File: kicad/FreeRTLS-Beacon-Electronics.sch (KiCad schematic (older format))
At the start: 0 parts

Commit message: Add DWM USB and STM to sch
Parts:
- added D?: PMEG3020EH, Diode_SMD:D_SOD-123F, symbol Diode:PMEG3020EH
- added J?: USB_B_Micro, symbol Connector:USB_B_Micro
- added U?: DWM1001, RF_Module:DecaWave_DWM1001, symbol RF_Module:DWM1001
- added U?: STM32F072CBTx, Package_QFP:LQFP-48_7x7mm_P0.5mm, symbol MCU_ST_STM32F0:STM32F072CBTx
- added U?: NCP1117-3.3_SOT223, Package_TO_SOT_SMD:SOT-223-3_TabPin2, symbol Regulator_Linear:NCP1117-3.3_SOT223
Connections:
- new net: U?.1 (GND), U?.11 (GND), U?.24 (GND), U?.34 (GND)
- new net: D?.2 (A), J?.1 (VBUS)
- new net: D?.1 (K), U?.3 (VI)
- no-connect marks 0 -> 28
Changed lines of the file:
@@
 Sheet 1 1
 Title "FreeRTLS Beacon Electronics"
-Date "2020-08-27"
+Date "2020-09-01"
 Rev "WIP!"
 Comp "FreeRTLS"
@@
 Comment4 ""
 $EndDescr
+$Comp
+L RF_Module:DWM1001 U?
+U 1 1 5F4EAC7B
+P 6400 2750
+F 0 "U?" H 6400 4031 50  0000 C CNN
+F 1 "DWM1001" H 6400 3940 50  0000 C CNN
+F 2 "RF_Module:DecaWave_DWM1001" H 7100 1800 50  0001 C CNN
+F 3 "https://www.decawave.com/sites/default/files/dwm1001_datasheet.pdf" H 7300 1950 50  0001 C CNN
+	1    6400 2750
+	1    0    0    -1
+$EndComp
+$Comp
+L MCU_ST_STM32F0:STM32F072CBTx U?
+U 1 1 5F4EB7E0
+P 4800 5600
+F 0 "U?" H 4750 4011 50  0000 C CNN
+F 1 "STM32F072CBTx" H 4750 3920 50  0000 C CNN
+F 2 "Package_QFP:LQFP-48_7x7mm_P0.5mm" H 4200 4200 50  0001 R CNN
+F 3 "http://www.st.com/st-web-ui/static/active/en/resource/technical/document/datasheet/DM00090510.pdf" H 4800 5600 50  0001 C CNN
+	1    4800 5600
+	1    0    0    -1
+$EndComp
+$Comp
+L Connector:USB_B_Micro J?
+U 1 1 5F4ED800
+P 1650 2900
+F 0 "J?" H 1707 3367 50  0000 C CNN
+F 1 "USB_B_Micro" H 1707 3276 50  0000 C CNN
+F 2 "" H 1800 2850 50  0001 C CNN
+F 3 "~" H 1800 2850 50  0001 C CNN
+	1    1650 2900
+	1    0    0    -1
+$EndComp
+$Comp
+L Regulator_Linear:NCP1117-3.3_SOT223 U?
+U 1 1 5F4F1B06
+P 3200 2700
+F 0 "U?" H 3200 2942 50  0000 C CNN
+F 1 "NCP1117-3.3_SOT223" H 3200 2851 50  0000 C CNN
+F 2 "Package_TO_SOT_SMD:SOT-223-3_TabPin2" H 3200 2900 50  0001 C CNN
+F 3 "http://www.onsemi.com/pub_link/Collateral/NCP1117-D.PDF" H 3300 2450 50  0001 C CNN
+	1    3200 2700
+	1    0    0    -1
+$EndComp
+NoConn ~ 4100 5400
+NoConn ~ 4100 5500
+NoConn ~ 4100 5600
+NoConn ~ 4100 5700
+NoConn ~ 4100 5800
+NoConn ~ 4100 5900
+NoConn ~ 4100 6000
+NoConn ~ 4100 6100
+NoConn ~ 4100 6200
+NoConn ~ 4100 6300
+NoConn ~ 4100 6400
+NoConn ~ 4100 6500
+NoConn ~ 4100 6600
+NoConn ~ 4100 6700
+NoConn ~ 4100 6800
+NoConn ~ 4100 6900
+NoConn ~ 4100 5000
+NoConn ~ 4100 5100
+NoConn ~ 4100 5200
+NoConn ~ 4100 4700
+NoConn ~ 4100 4800
+NoConn ~ 5400 6200
+NoConn ~ 5400 5900
+NoConn ~ 5400 6000
+NoConn ~ 5400 6100
+NoConn ~ 5400 5700
+NoConn ~ 5400 6900
+NoConn ~ 1950 3100
+$Comp
+L Diode:PMEG3020EH D?
+U 1 1 5F4FD35F
+P 2200 2700
+F 0 "D?" H 2200 2484 50  0000 C CNN
+F 1 "PMEG3020EH" H 2200 2575 50  0000 C CNN
+F 2 "Diode_SMD:D_SOD-123F" H 2200 2525 50  0001 C CNN
+F 3 "https://assets.nexperia.com/documents/data-sheet/PMEG3020EH_EJ.pdf" H 2200 2700 50  0001 C CNN
+	1    2200 2700
+	-1   0    0    1
+$EndComp
+Wire Wire Line
+	1950 2700 2050 2700
+Wire Wire Line
+	2350 2700 2900 2700
 $EndSCHEMATC

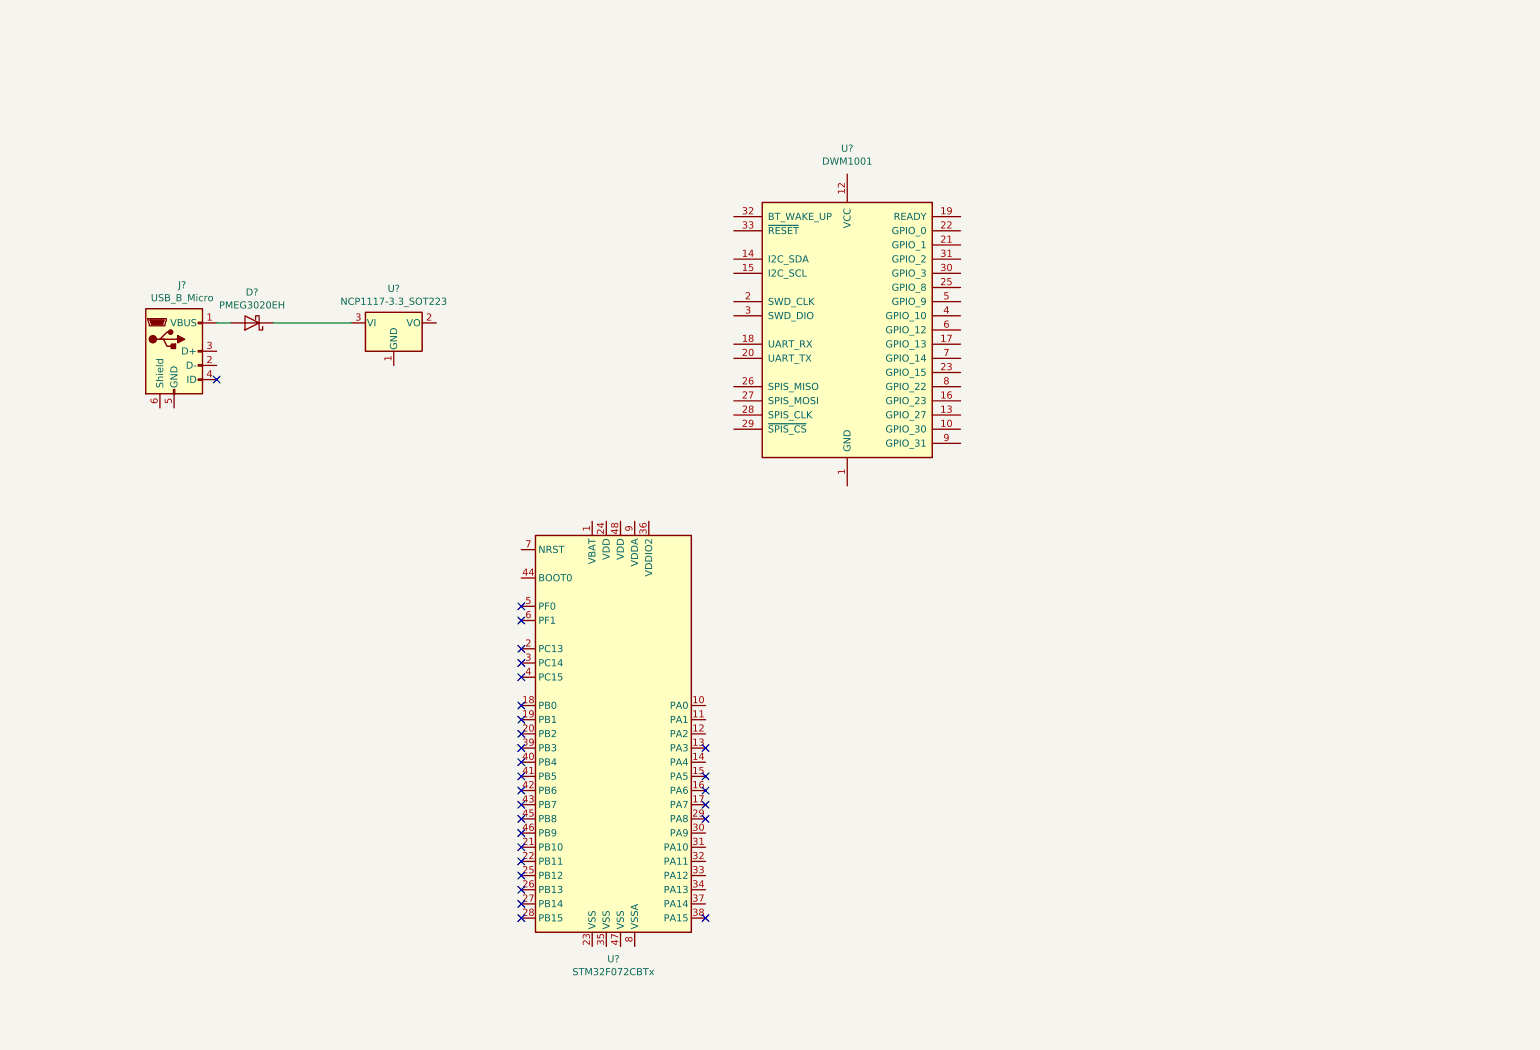
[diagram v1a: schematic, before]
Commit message: Add STM32 connections
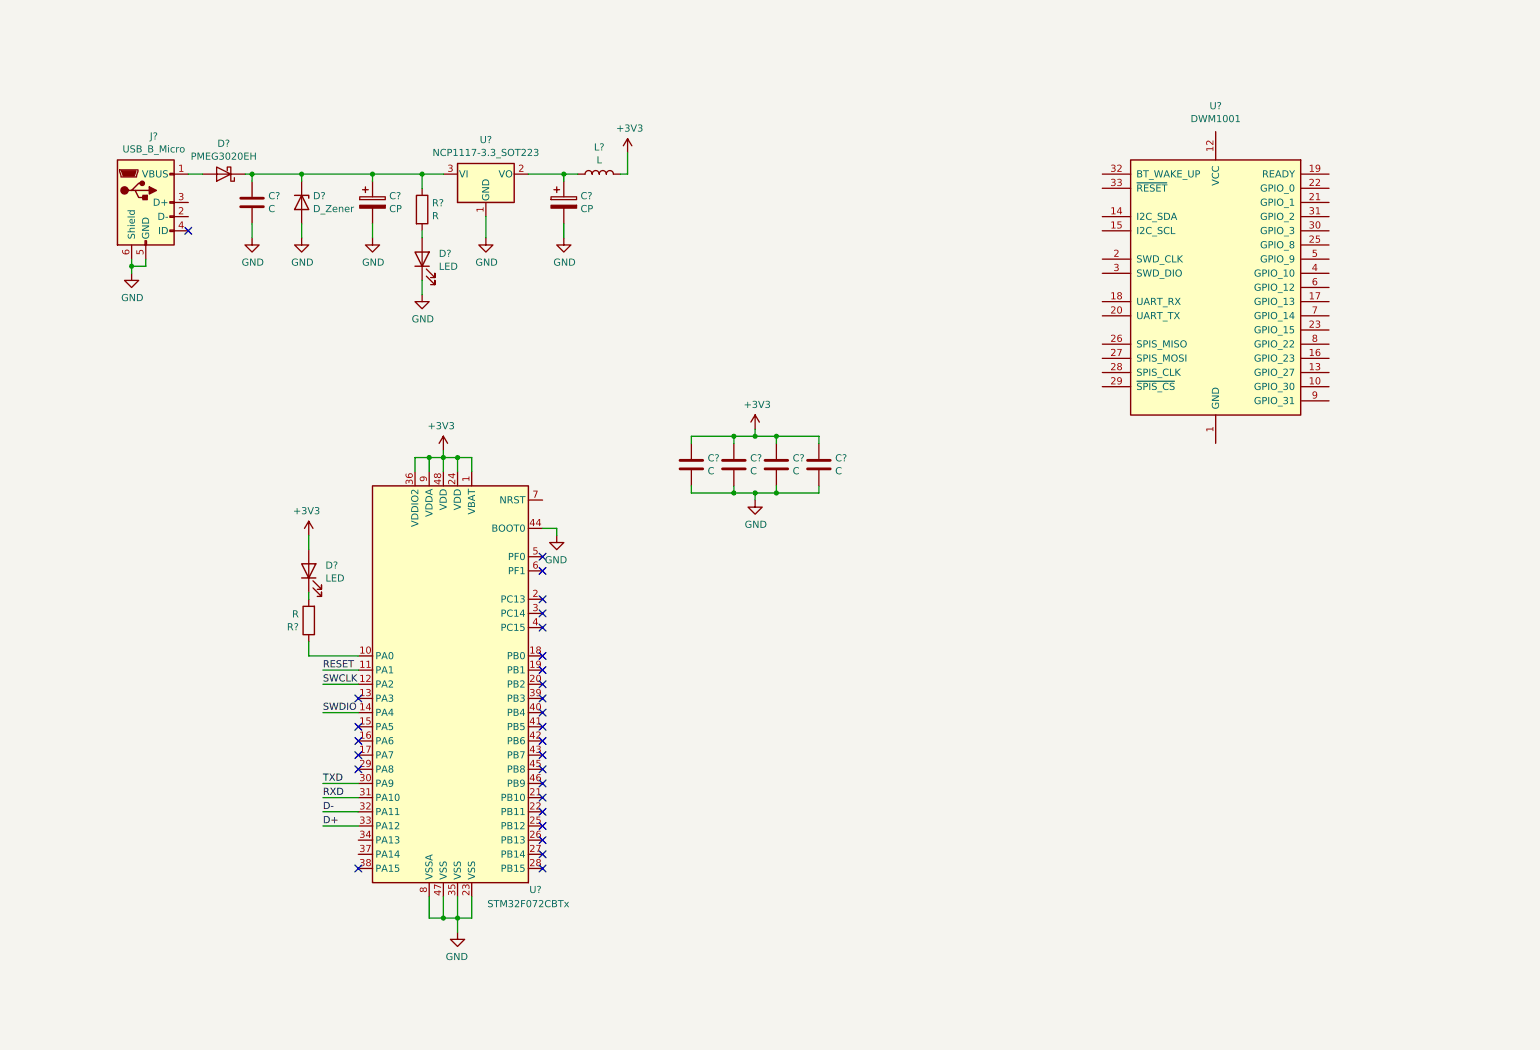
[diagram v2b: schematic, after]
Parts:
- added C? (x5): C, symbol Device:C
- added C? (x2): CP, symbol Device:CP
- added D?: D_Zener, symbol Device:D_Zener
- added D? (x2): LED, symbol Device:LED
- added L?: L, symbol Device:L
- added R? (x2): R, symbol Device:R
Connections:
- net +3V3: now reaches U?.1 (VBAT)
- net +3V3: now also U?.24 (VDD), U?.36 (VDDIO2), U?.48 (VDD), U?.9 (VDDA), C?.1, C?.1, C?.1, C?.1, D?.2 (A), L?.2
- net at U?.10 (PA0): now also R?.1
- net RESET: now reaches U?.11 (PA1)
- net SWCLK: now reaches U?.12 (PA2)
- net SWDIO: now reaches U?.14 (PA4)
- net GND: now reaches U?.23 (VSS)
- net GND: now also J?.5 (GND), J?.6 (Shield), U?.1 (GND), U?.35 (VSS), U?.44 (BOOT0), U?.47 (VSS), U?.8 (VSSA), C?.2, C?.2, C?.2, C?.2, C?.2, C?.2, C?.2, D?.1 (K), D?.2 (A)
- net TXD: now reaches U?.30 (PA9)
- net RXD: now reaches U?.31 (PA10)
- net D-: now reaches U?.32 (PA11)
- net D+: now reaches U?.33 (PA12)
- net at U?.2 (VO): now also C?.1, L?.1
- net at D?.1 (K), U?.3 (VI): now also C?.1, C?.1, D?.1 (K), R?.1
- new net: D?.2 (A), R?.2
- new net: D?.1 (K), R?.2
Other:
- moved on the sheet: D?, J?, U?

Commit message: Complete USB-STM connections
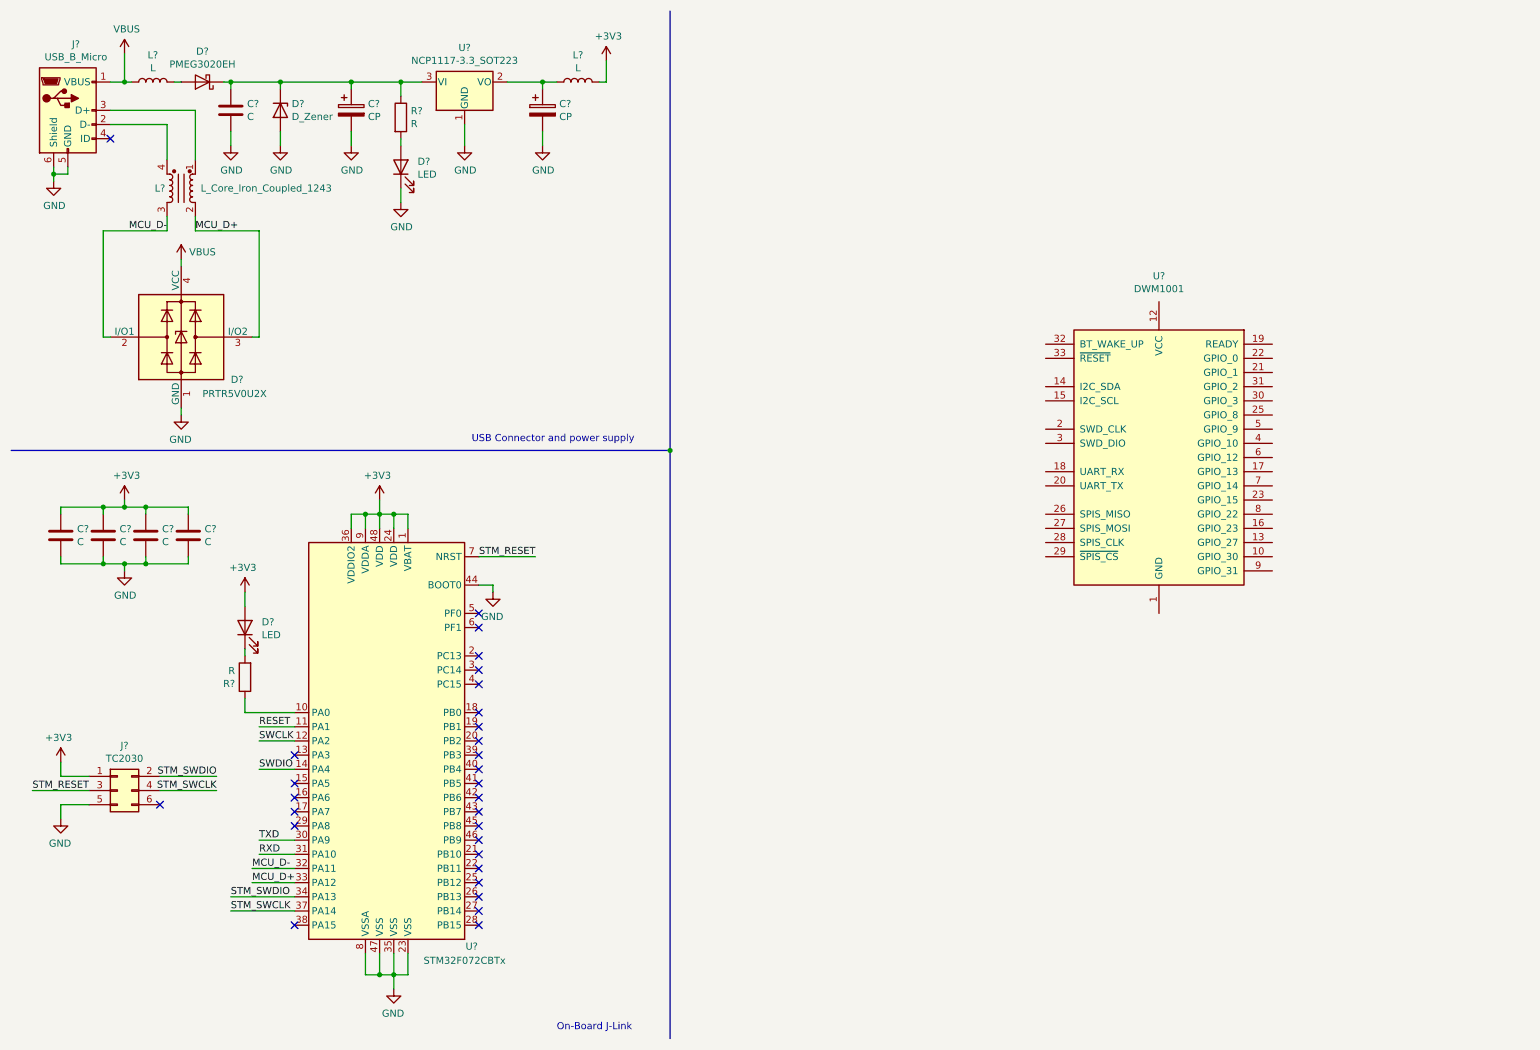
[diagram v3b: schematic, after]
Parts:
- added D?: PRTR5V0U2X, Package_TO_SOT_SMD:SOT-143, symbol Power_Protection:PRTR5V0U2X
- added J?: TC2030, Connector:Tag-Connect_TC2030-IDC-FP_2x03_P1.27mm_Vertical, symbol Connector_Generic:Conn_02x03_Odd_Even
- added L?: L_Core_Iron_Coupled_1243, symbol Device:L_Core_Iron_Coupled_1243
- added L?: L, symbol Device:L
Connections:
- net +3V3: now also J?.1 (Pin_1)
- net GND: now also D?.1 (GND), J?.5 (Pin_5)
- net STM_SWDIO: now reaches U?.34 (PA13)
- net STM_SWDIO: now also J?.2 (Pin_2)
- net STM_SWCLK: now reaches U?.37 (PA14)
- net STM_SWCLK: now also J?.4 (Pin_4)
- net STM_RESET: now reaches U?.7 (NRST)
- net STM_RESET: now also J?.3 (Pin_3)
- net at D?.2 (A): now also L?.2; no longer J?.1 (VBUS)
- net at J?.2 (D-): now also L?.4
- net at J?.3 (D+): now also L?.1
- net D+ renamed MCU_D+
- net MCU_D+: now also D?.3 (I/O2), L?.2
- net D- renamed MCU_D-
- net MCU_D-: now also D?.2 (I/O1), L?.3
- new net VBUS: D?.4 (VCC), J?.1 (VBUS), L?.1
- no-connect marks 28 -> 29
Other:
- note added: "On-Board J-Link"
- note added: "USB Connector and power supply"
- moved on the sheet: C?, D?, J?, L?, R?, U?
